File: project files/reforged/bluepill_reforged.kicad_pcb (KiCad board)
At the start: 2 copper layers, 22.9 x 53.3 mm, 39 parts, among them J1 USB_C_Receptacle_USB2.0, J2 Left Castellation, J3 Cortex debug, J4 Right Castellation, SW1 Boot0, SW2 Reset, U1 AMS1117-3.3, U2 STM32F103C8Tx, Y1 8MHz, Y2 32768Hz

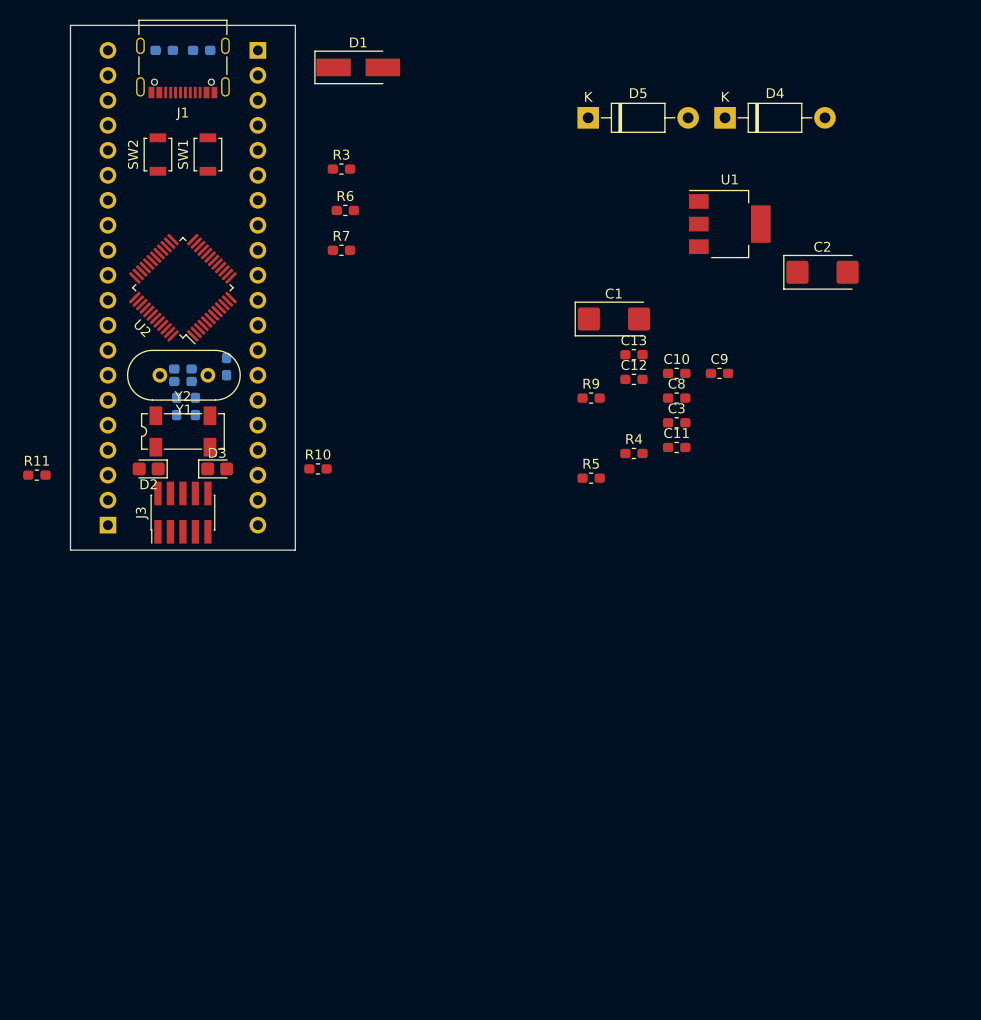
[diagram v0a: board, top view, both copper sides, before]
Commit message: replaced SWD 10 with 14
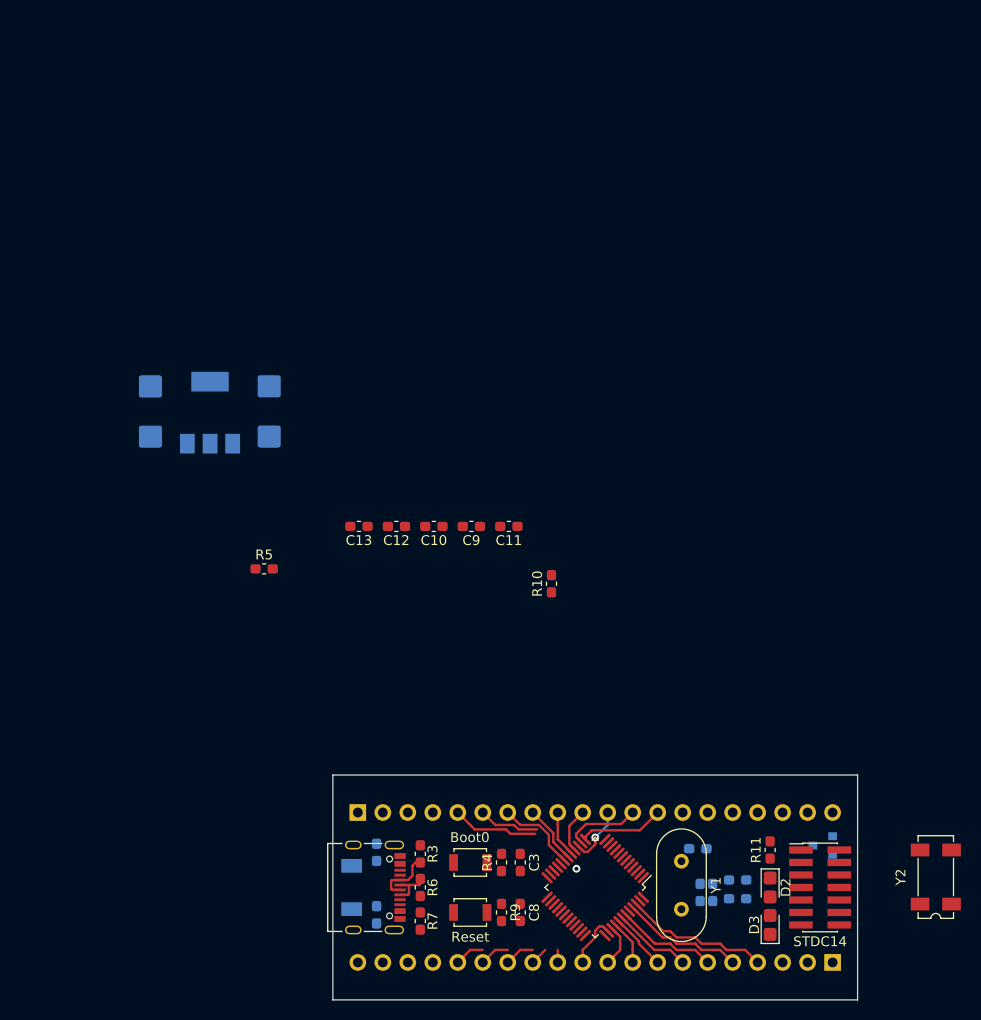
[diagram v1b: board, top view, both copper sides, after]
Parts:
- removed D5: 1N5819, Diode_THT:D_DO-41_SOD81_P10.16mm_Horizontal
- C1, C2, U1: moved to B.Cu
- C3, C8: value 1uF -> 100nf
- D1: footprint Diode_SMD:D_SMA_Handsoldering -> Diode_SMD:D_SOD-128; moved to B.Cu
- D2: value Green -> PC13
- D4: value 1N5819 -> BAT54C; footprint Diode_THT:D_DO-41_SOD81_P10.16mm_Horizontal -> Package_TO_SOT_SMD:SOT-23; moved to B.Cu
- J3: value Cortex debug -> STDC14; footprint Connector_PinHeader_1.27mm:PinHeader_2x05_P1.27mm_Vertical_SMD -> Connector_PinHeader_1.27mm:PinHeader_2x07_P1.27mm_Vertical_SMD
- moved R2 90.5 mm to (132.7, 141.2), turned to 270 degrees
- moved Y2 88.9 mm to (189.6, 137.4), turned to 90 degrees
- moved J2 86.0 mm to (179.1, 146.1), turned to 90 degrees
- moved J1 85.6 mm to (132.6, 138.4), turned to 270 degrees
- moved R11 83.7 mm to (172.7, 134.6), turned to 90 degrees
- moved R1 83.4 mm to (132.7, 134.9), turned to 90 degrees
- moved D1 83.4 mm to (130.2, 138.4), turned to 90 degrees
- moved SW2 83.3 mm to (142.2, 141.0), turned to 0 degrees
- moved J4 78.1 mm to (130.8, 130.8), turned to 270 degrees
- moved SW1 76.7 mm to (142.2, 135.9), turned to 0 degrees
- moved D2 76.2 mm to (172.7, 138.4), turned to 270 degrees
- moved C7 75.9 mm to (169.4, 139.6), turned to 180 degrees
- moved J3 75.1 mm to (177.8, 138.4), turned to 0 degrees
- moved R8 74.8 mm to (166.9, 138.9), turned to 90 degrees
- moved C4 74.8 mm to (165.6, 138.9), turned to 90 degrees
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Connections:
- D4 pad 1: VBAT_Protected -> +BATT
- D4 pad 2: +BATT -> +3V3
- J3 pad 1: +3V3 -> Net-(J3-Pad1)
- J3 pad 10: NRST -> Net-(J3-Pad10)
- J3 pad 2: PA13 -> Net-(J3-Pad2)
- J3 pad 3: GNDREF -> +3V3
- J3 pad 4: PA14 -> PA13
- J3 pad 6: PB3 -> PA14
- J3 pad 7: Net-(J3-Pad7) -> GNDREF
- J3 pad 8: Net-(J3-Pad8) -> PB3
- J3 pad 9: GNDREF -> Net-(J3-Pad9)
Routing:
- net PB9: track 0.00 -> 14.8 mm
- net PB8: track 0.00 -> 12.4 mm
- net PB7: track 0.00 -> 10.4 mm
- net PB11: track 0.00 -> 8.81 mm
- net PA3: track 0.00 -> 8.64 mm
- net PB1: track 0.00 -> 8.38 mm
- net PB6: track 0.00 -> 8.02 mm
- net PA4: track 0.00 -> 7.79 mm
- net PB10: track 0.00 -> 6.24 mm
- net D-: track 0.00 -> 6.11 mm
- net PA5: track 0.00 -> 6.02 mm, vias 0 -> 1
- net PB0: track 0.00 -> 5.98 mm
- net PB5: track 0.00 -> 5.80 mm
- net PA15: track 0.00 -> 5.52 mm
- net PA7: track 0.00 -> 4.72 mm
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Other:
- board size 22.9 x 53.3 mm -> 53.3 x 22.9 mm

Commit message: minor
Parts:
- added C14: 100n, Capacitor_SMD:C_0603_1608Metric_Pad1.05x0.95mm_HandSolder, F.Cu at (138.0, 135.3)
- R1, R2: moved to F.Cu
- moved C9 56.3 mm to (189.0, 133.3)
- moved J4 48.3 mm to (179.1, 130.8), turned to 90 degrees
- moved C1 32.9 mm to (120.5, 121.2)
- moved C2 32.9 mm to (132.6, 121.2)
- moved U1 32.9 mm to (126.4, 121.3)
- moved R5 24.8 mm to (142.2, 119.4)
- moved C10 24.8 mm to (159.5, 115.1)
- moved C11 24.8 mm to (167.1, 115.1)
- moved C12 24.8 mm to (155.7, 115.1)
- moved C13 24.8 mm to (151.9, 115.1)
- moved R10 24.8 mm to (171.4, 120.9)
- moved Y2 20.4 mm to (169.2, 138.2)
- moved R2 6.32 mm to (138.0, 137.8), turned to 0 degrees
- moved SW2 5.75 mm to (141.6, 135.3), turned to 90 degrees
- moved C8 5.75 mm to (146.7, 135.3)
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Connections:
- J4 pad 1: GNDREF -> +BATT
- J4 pad 10: PA6 -> PA5
- J4 pad 11: PA5 -> PA6
- J4 pad 12: PA4 -> PA7
- J4 pad 13: PA3 -> PB0
- J4 pad 14: PA2 -> PB1
- J4 pad 15: PA1 -> PB10
- J4 pad 16: PA0 -> PB11
- J4 pad 17: PC15 -> NRST
- J4 pad 18: PC14 -> +3V3
- J4 pad 19: PC13 -> GNDREF
- J4 pad 2: GNDREF -> PC13
- J4 pad 20: +BATT -> GNDREF
- J4 pad 3: +3V3 -> PC14
- J4 pad 4: NRST -> PC15
- J4 pad 5: PB11 -> PA0
- J4 pad 6: PB10 -> PA1
- J4 pad 7: PB1 -> PA2
- J4 pad 8: PB0 -> PA3
- J4 pad 9: PA7 -> PA4
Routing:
- net PB9: track 14.8 -> 0.00 mm
- net PB8: track 12.4 -> 0.00 mm
- net PB7: track 10.4 -> 0.00 mm
- net PB11: track 8.81 -> 0.00 mm
- net PA3: track 8.64 -> 0.00 mm
- net PB1: track 8.38 -> 0.00 mm
- net PB6: track 8.02 -> 0.00 mm
- net PA4: track 7.79 -> 0.00 mm
- net PB10: track 6.24 -> 0.00 mm
- net D-: track 6.11 -> 0.00 mm
- net PA5: track 6.02 -> 0.00 mm, vias 1 -> 0
- net PB0: track 5.98 -> 0.00 mm
- net PB5: track 5.80 -> 0.00 mm
- net PA15: track 5.52 -> 0.00 mm
- net PA7: track 4.72 -> 0.00 mm
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
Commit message: minor updates
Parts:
- added F1: 1A, Fuse:Fuse_0805_2012Metric, B.Cu at (132.1, 138.4)
- C9: moved to B.Cu
- D1: value Protection -> 1A
- moved C3 20.3 mm to (146.1, 120.7)
- moved C8 18.9 mm to (158.8, 120.7)
- moved R5 14.4 mm to (145.4, 133.4)
- moved C9 12.8 mm to (176.8, 137.2), turned to 0 degrees
- moved R9 8.24 mm to (136.8, 133.3), turned to 180 degrees
- moved C1 6.84 mm to (123.1, 114.8)
- moved U1 6.84 mm to (128.9, 114.9)
- moved C2 6.84 mm to (135.1, 114.8)
- moved C11 5.41 mm to (164.2, 110.5)
- moved R2 4.87 mm to (136.8, 142.5)
- moved R8 4.35 mm to (162.6, 138.4)
- moved R4 2.01 mm to (145.4, 142.9), turned to 180 degrees
- moved R3 1.71 mm to (136.8, 137.9)
- moved R6 1.55 mm to (136.8, 139.4)
- moved R7 1.42 mm to (136.8, 141.0), turned to 180 degrees
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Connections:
- D1 pad 2: VBUS -> Net-(D1-Pad2)
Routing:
- net PB12: track 0.00 -> 23.0 mm
- net PB13: track 0.00 -> 20.7 mm
- net PB14: track 0.00 -> 18.3 mm
- net PB15: track 0.00 -> 15.8 mm
- net PA8: track 0.00 -> 12.7 mm
- net PB11: track 0.00 -> 12.7 mm
- net PA1: track 0.00 -> 11.4 mm
- net PB10: track 0.00 -> 10.5 mm
- net PA9: track 0.00 -> 10.3 mm
- net PB7: track 0.00 -> 10.3 mm
- net PB1: track 0.00 -> 9.18 mm
- net PA2: track 0.00 -> 9.15 mm
- net PA3: track 0.00 -> 8.48 mm
- net PA10: track 0.00 -> 8.06 mm
- net PB6: track 0.00 -> 8.03 mm
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- added copper zone on B.Cu, net GNDREF
- added copper zone on F.Cu, net GNDREF
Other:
- net class Default: trace_width 0.25 -> 0.2
- net class Power added: clearance 0.635, trace_width 0.635, via_dia 0.8, via_drill 0.4

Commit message: Update bluepill_reforged.kicad_pcb
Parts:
- added U3: STM32F103CBUx, Package_DFN_QFN:QFN-48-1EP_7x7mm_P0.5mm_EP5.6x5.6mm, F.Cu at (153.7, 138.4)

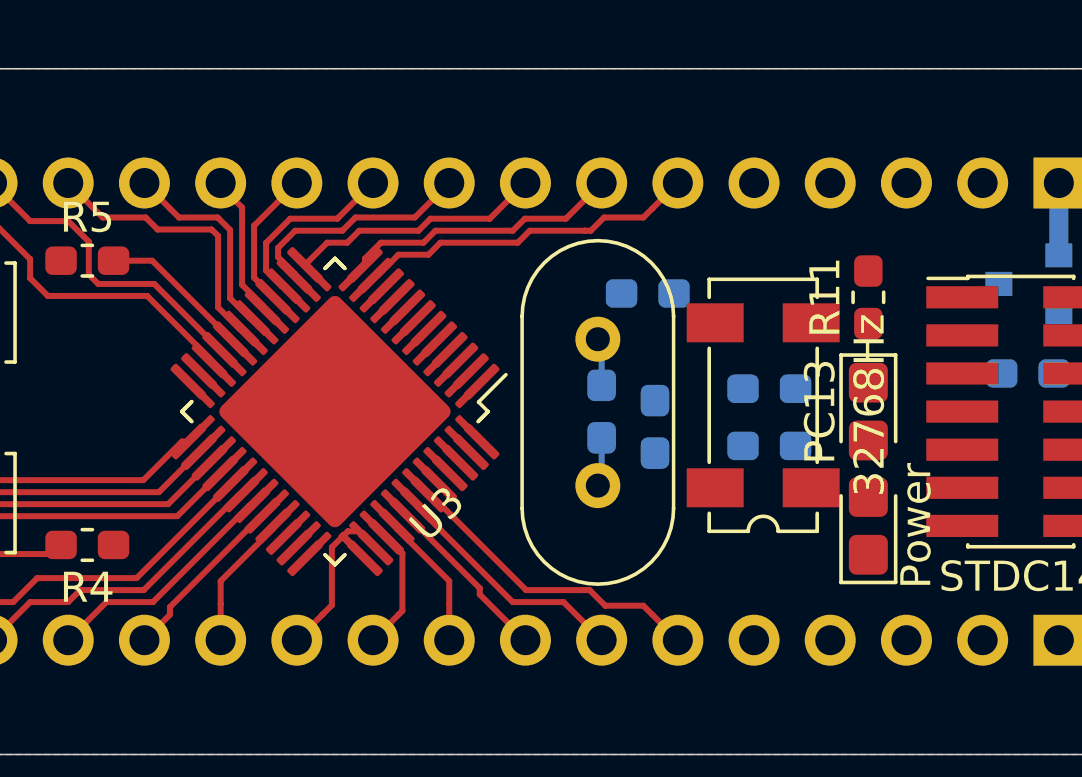
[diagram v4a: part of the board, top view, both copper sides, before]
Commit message: replaced crystal with smd
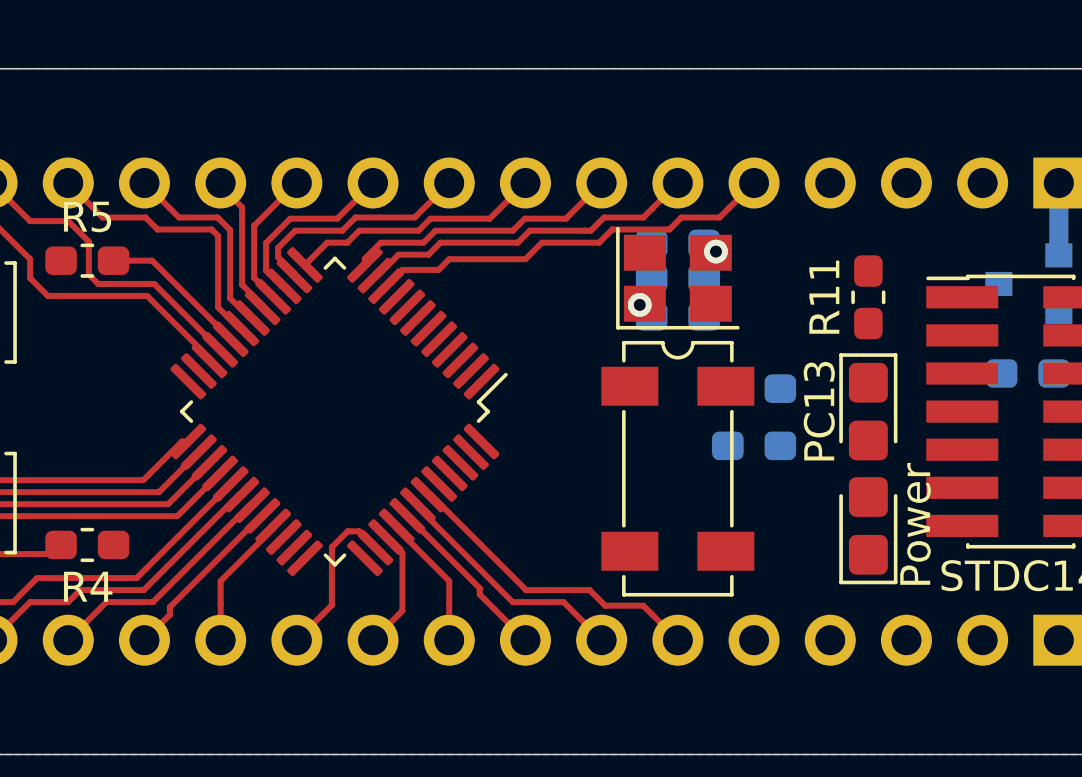
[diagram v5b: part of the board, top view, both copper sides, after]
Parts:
- removed U3: STM32F103CBUx, Package_DFN_QFN:QFN-48-1EP_7x7mm_P0.5mm_EP5.6x5.6mm
- R8: value 10M [N/A] -> 10M[N/A]
- Y1: value 8MHz -> 8Mhz,TSX-3225; footprint Crystal:Crystal_HC49-4H_Vertical -> Crystal:Crystal_SMD_3225-4Pin_3.2x2.5mm
- Y2: value 32768Hz -> MC-306, 32768Hz
- moved R8 5.12 mm to (165.1, 134.0), turned to 0 degrees
- moved C4 3.76 mm to (165.1, 135.3), turned to 0 degrees
- moved Y2 3.55 mm to (165.1, 140.3), turned to 270 degrees
- moved Y1 3.35 mm to (165.1, 134.0), turned to 0 degrees
- moved C6 1.93 mm to (165.1, 132.8)
- moved C5 0.51 mm to (167.6, 137.7)
- moved C7 0.51 mm to (167.6, 139.6)
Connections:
- Y1 pad 1: OSCOUT -> OSCIN
- Y1 pad 2: OSCIN -> GNDREF
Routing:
- net PA0: track 0.00 -> 13.7 mm
- net OSCIN: track 1.64 -> 0.19 mm, vias 0 -> 1
- net OSCOUT: track 1.59 -> 0.19 mm, vias 0 -> 1

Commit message: Update bluepill_reforged.kicad_pcb
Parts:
- D2, D3: footprint LED_SMD:LED_0805_2012Metric_Castellated -> LED_SMD:LED_0603_1608Metric_Castellated
- moved C5 4.65 mm to (163.8, 140.3), turned to 270 degrees
- moved C4 2.29 mm to (163.2, 134.0), turned to 90 degrees
- moved C6 2.22 mm to (167.0, 134.0), turned to 270 degrees
- moved C7 1.48 mm to (166.4, 140.3), turned to 270 degrees
- moved D2 1.27 mm to (170.2, 138.4)
- moved D3 1.27 mm to (170.2, 142.2)
- moved R11 1.27 mm to (170.2, 134.6)
- moved J3 0.63 mm to (175.9, 138.4)
- moved D4 0.19 mm to (176.8, 134.0)
- turned R8 to 90 degrees
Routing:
- net +BATT: track 2.41 -> 0.00 mm
- net OSCOUT: vias 1 -> 0
- net OSCIN: vias 1 -> 0

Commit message: re-arrangements
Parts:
- C1, C2: footprint Capacitor_Tantalum_SMD:CP_EIA-6032-20_AVX-F_Pad2.25x2.35mm_HandSolder -> Capacitor_Tantalum_SMD:CP_EIA-3528-12_Kemet-T
- C10, C11, C12, C13, C14, C3, C8, R10, R11, R4, R5: moved to B.Cu
- moved C2 28.5 mm to (137.2, 143.3), turned to 0 degrees
- moved C12 28.1 mm to (151.8, 142.9)
- moved C11 26.2 mm to (155.6, 135.3), turned to 0 degrees
- moved U1 25.6 mm to (139.1, 138.4), turned to 0 degrees
- moved C10 24.3 mm to (155.6, 139.1)
- moved C1 23.5 mm to (137.2, 133.6), turned to 0 degrees
- moved C3 23.1 mm to (142.5, 143.5), turned to 180 degrees
- moved C13 22.2 mm to (150.3, 137.2)
- moved C8 21.9 mm to (142.5, 135.3), turned to 0 degrees
- moved R10 13.8 mm to (170.2, 134.6), turned to 270 degrees
- moved R11 6.48 mm to (171.4, 141.0), turned to 180 degrees
- moved C14 6.46 mm to (132.5, 139.7)
- moved R4 3.20 mm to (142.5, 141.6), turned to 0 degrees
- moved R5 2.94 mm to (142.5, 133.3)
- moved R2 2.57 mm to (137.2, 140.0)
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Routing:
- net PB12: track 23.0 -> 0.00 mm
- net PB13: track 20.7 -> 0.00 mm
- net PB14: track 18.3 -> 0.00 mm
- net PB15: track 15.8 -> 0.00 mm
- net PA0: track 13.7 -> 0.00 mm
- net PA8: track 12.7 -> 0.00 mm
- net PB11: track 12.7 -> 0.00 mm
- net PA1: track 11.4 -> 0.00 mm
- net PB10: track 10.5 -> 0.00 mm
- net PA9: track 10.3 -> 0.00 mm
- net PB7: track 10.3 -> 0.00 mm
- net PB1: track 9.18 -> 0.00 mm
- net PA2: track 9.15 -> 0.00 mm
- net PA3: track 8.48 -> 0.00 mm
- net PA10: track 8.06 -> 0.00 mm
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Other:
- board text added: "+3.3"
- board text added: "+5"
- board text added: "A0"
- board text added: "A1"
- board text added: "A10"
- board text added: "A11"
- board text added: "A12"
- board text added: "A15"
- board text added: "A2"
- board text added: "A3"
- board text added: "A4"
- board text added: "A5"
- board text added: "A6"
- board text added: "A7"
- board text added: "A8"
- board text added: "A9"
- board text added: "B0"
- board text added: "B1"
- board text added: "B10"
- board text added: "B11"
- board text added: "B12"
- board text added: "B13"
- board text added: "B14"
- board text added: "B15"
- board text added: "B3"
- board text added: "B4"
- board text added: "B5"
- board text added: "B6"
- board text added: "B7"
- board text added: "B8"
- board text added: "B9"
- board text added: "BAT"
- board text added: "C13"
- board text added: "C14"
- board text added: "C15"
- board text added: "G"
- board text added: "~R"

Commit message: updates
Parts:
- turned R7 to 0 degrees
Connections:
- net GNDREF renamed GNDD
- R7 pad 1: +3V3 -> VBUS
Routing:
- net D-: track 0.00 -> 5.41 mm
- net D+: track 0.00 -> 5.41 mm
- net PA12: track 0.00 -> 4.35 mm
- net Net-(J1-PadA5): track 0.00 -> 3.58 mm
- net VBUS: track 0.00 -> 2.73 mm
- net Net-(J1-PadB5): track 0.00 -> 2.55 mm
- added copper zone on B.Cu, net GNDREF
- added copper zone on F.Cu, net GNDREF
- removed copper zone on B.Cu, net GNDD
- removed copper zone on F.Cu, net GNDD
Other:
- board text added: "Vin"
- board text removed: "+5"
